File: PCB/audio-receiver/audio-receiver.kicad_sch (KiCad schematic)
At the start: 0 parts

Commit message: create amplifier schematic
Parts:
- added C1: 10uF, symbol Device:C_Polarized
- added C2, C4, C8: 100uF, symbol Device:C_Polarized
- added C3: 100pF, symbol Device:C_Small
- added C5: 2200uF, symbol Device:C_Polarized
- added C6: 33uF, symbol Device:C_Polarized
- added C7: 100nF, symbol Device:C
- added D1, D2, D3, D4: 1N4148, symbol Device:D
- added D5, D6, D7, D8: UF4004, symbol Device:D
- added F1: 1A, symbol Device:Fuse
- added Q1: BC559, Package_TO_SOT_THT:TO-92_Inline, symbol Transistor_BJT:BC559
- added Q2, Q3: BC639, symbol Device:Q_NPN
- added Q4: BC640, symbol Device:Q_PNP
- added Q5: MJE3055, symbol Device:Q_NPN
- added Q6: MJE2955, symbol Device:Q_PNP
- added R1, R2: 33k, symbol Device:R_US
- added R10, R13, R9: 2R7, symbol Device:R_US
- added R11: 12k, symbol Device:R_US
- added R12, R3, R6, R7: 2k2, symbol Device:R_US
- added R4: 100R, symbol Device:R_US
- added R5: 1k, symbol Device:R_US
- added R8: 560, symbol Device:R_US
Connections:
- new net: C8.1, F1.1, Q3.C, Q5.C, R11.2, R6.1
- new net: D1.2 (A), Q3.B, R7.2
- new net: Q3.E, Q5.B, R8.1
- new net: C1.1, Q1.2 (B), R1.2, R2.1
- new net: D6.1 (K), D8.1 (K), Q6.E, R10.2
- new net: C3.2, D4.1 (K), Q2.C, Q4.B
- new net: D3.1 (K), D4.2 (A)
- new net: D5.2 (A), D7.2 (A), Q5.E, R9.1
- new net: C3.1, Q1.1 (C), Q2.B, R5.1
- new net: C2.1, Q1.3 (E), R3.1
- new net: C2.2, R12.1, R4.1
- new net: D2.1 (K), D3.2 (A)
- new net: D1.1 (K), D2.2 (A)
- new net: C6.1, R1.1, R11.1
- new net: Q4.E, Q6.B, R8.2
- new net: C4.1, R6.2, R7.1
- new net: C7.2, R13.1
- new net FB_DC: C4.2, C5.1, D5.1 (K), D6.2 (A), D7.1 (K), D8.2 (A), R10.1, R3.2, R9.2
- new net GND: C6.2, C8.2, Q2.E, Q4.C, Q6.C, R13.2, R2.2, R4.2, R5.2
- new net VCC: F1.2
- new net VIN: C1.2
- new net VOUT: C5.2, C7.1, R12.2
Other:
- note added: "FB_AC"

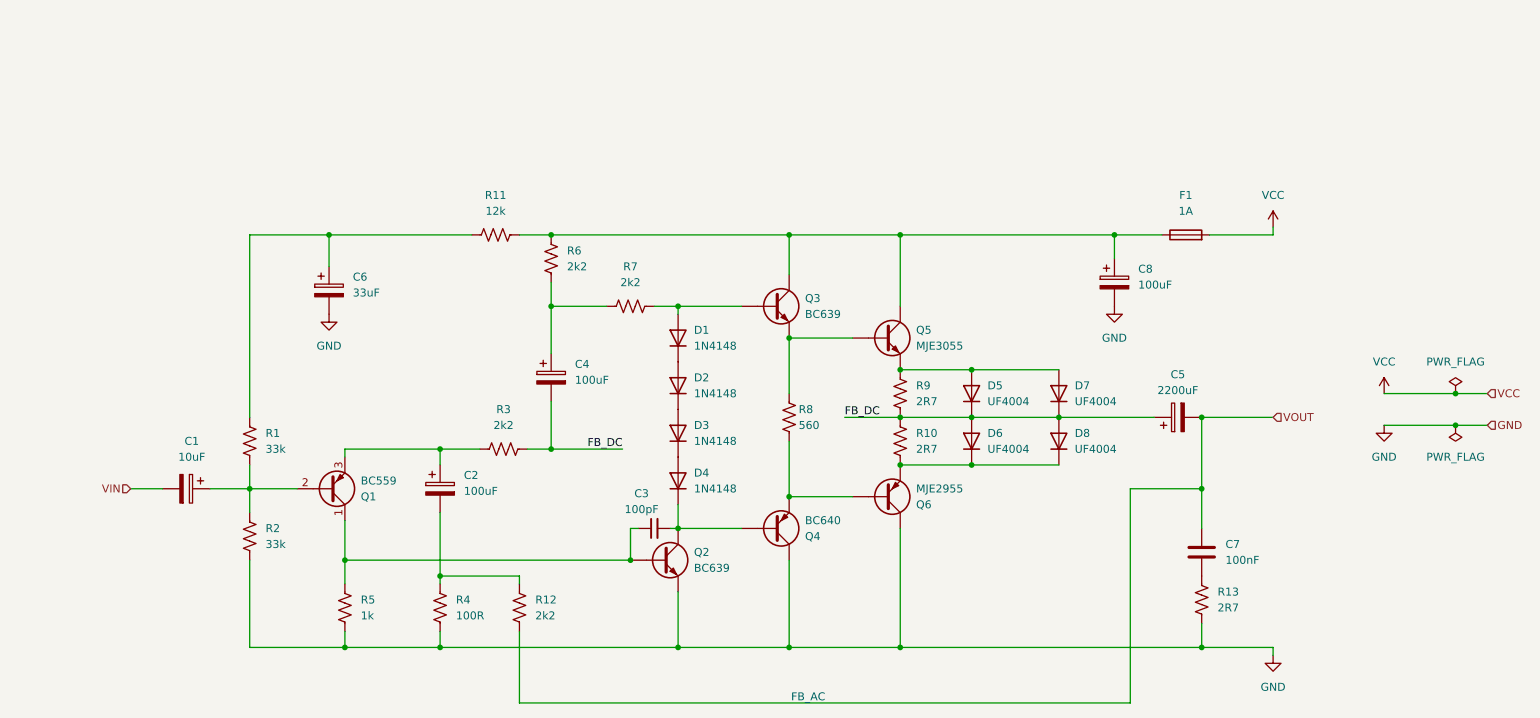
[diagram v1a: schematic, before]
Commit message: edit amplifier schematic
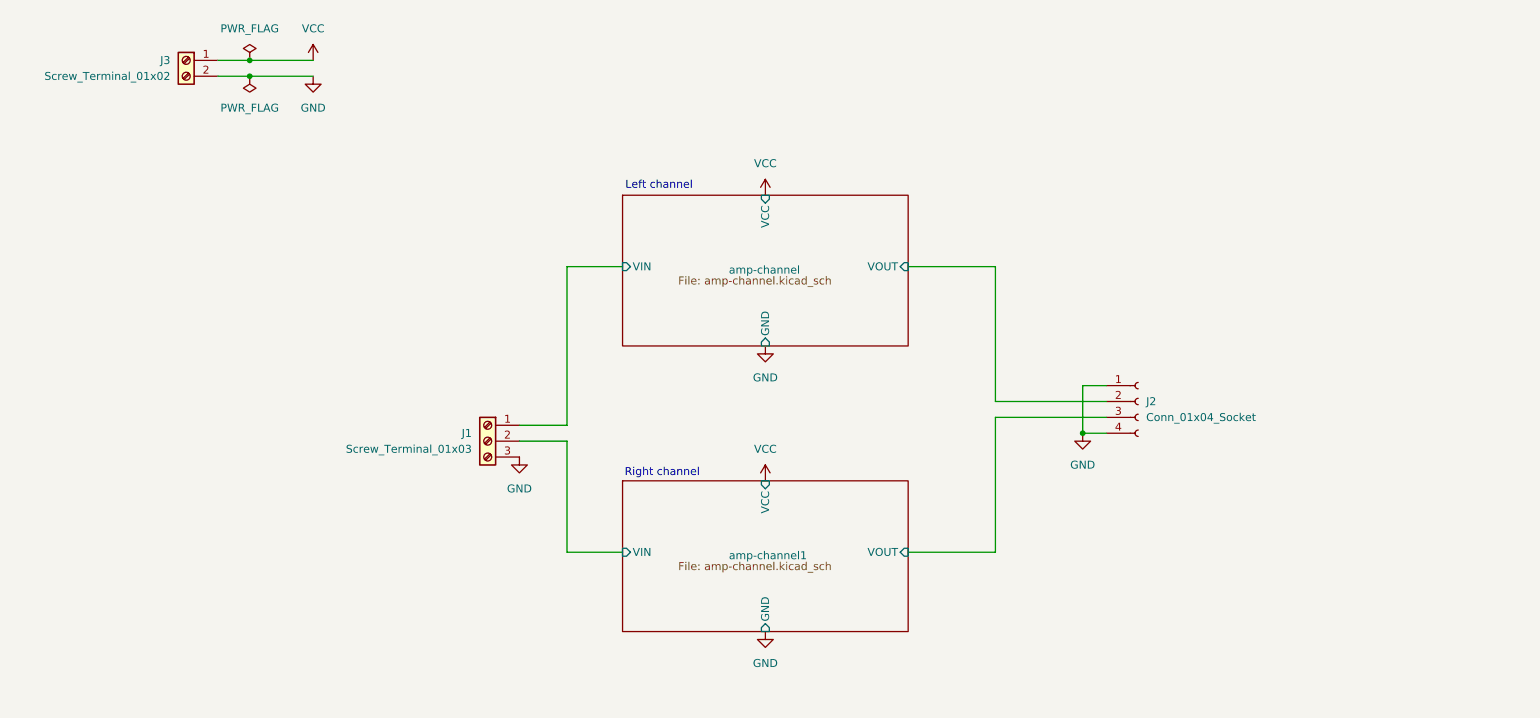
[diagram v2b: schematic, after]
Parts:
- removed C1: 10uF, symbol Device:C_Polarized
- removed C2, C4, C8: 100uF, symbol Device:C_Polarized
- removed C3: 100pF, symbol Device:C_Small
- removed C5: 2200uF, symbol Device:C_Polarized
- removed C6: 33uF, symbol Device:C_Polarized
- removed C7: 100nF, symbol Device:C
- removed D1, D2, D3, D4: 1N4148, symbol Device:D
- removed D5, D6, D7, D8: UF4004, symbol Device:D
- removed F1: 1A, symbol Device:Fuse
- removed Q1: BC559, Package_TO_SOT_THT:TO-92_Inline, symbol Transistor_BJT:BC559
- removed Q2, Q3: BC639, symbol Device:Q_NPN
- removed Q4: BC640, symbol Device:Q_PNP
- removed Q5: MJE3055, symbol Device:Q_NPN
- removed Q6: MJE2955, symbol Device:Q_PNP
- removed R1, R2: 33k, symbol Device:R_US
- removed R10, R13, R9: 2R7, symbol Device:R_US
- removed R11: 12k, symbol Device:R_US
- removed R12, R3, R6, R7: 2k2, symbol Device:R_US
- removed R4: 100R, symbol Device:R_US
- removed R5: 1k, symbol Device:R_US
- removed R8: 560, symbol Device:R_US
- added J1: Screw_Terminal_01x03, symbol Connector:Screw_Terminal_01x03
- added J2: Conn_01x04_Socket, symbol Connector:Conn_01x04_Socket
- added J3: Screw_Terminal_01x02, symbol Connector:Screw_Terminal_01x02
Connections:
- net GND: now also J1.3 (Pin_3), J2.1 (Pin_1), J2.4 (Pin_4), J3.2 (Pin_2)
- net VCC: now also J3.1 (Pin_1)
- new net amp-channel/VIN: J1.1 (Pin_1)
- new net amp-channel/VOUT: J2.2 (Pin_2)
- new net amp-channel1/VIN: J1.2 (Pin_2)
- new net amp-channel1/VOUT: J2.3 (Pin_3)
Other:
- added sheet amp-channel (amp-channel.kicad_sch)
- added sheet amp-channel1 (amp-channel.kicad_sch)
- note added: "Left channel"
- note added: "Right channel"
- note removed: "FB_AC"

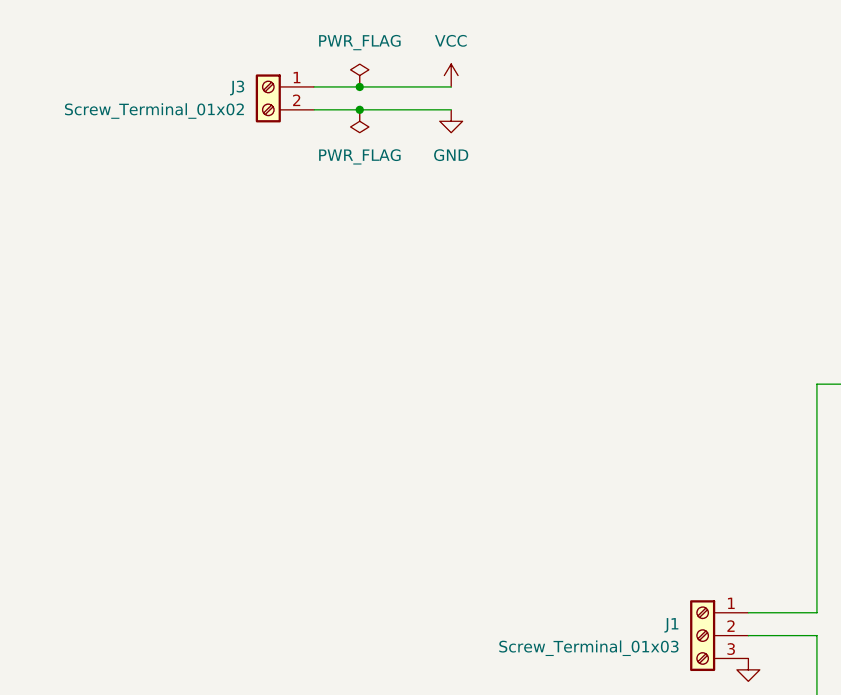
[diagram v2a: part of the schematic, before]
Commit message: update schematic and start work on BOM
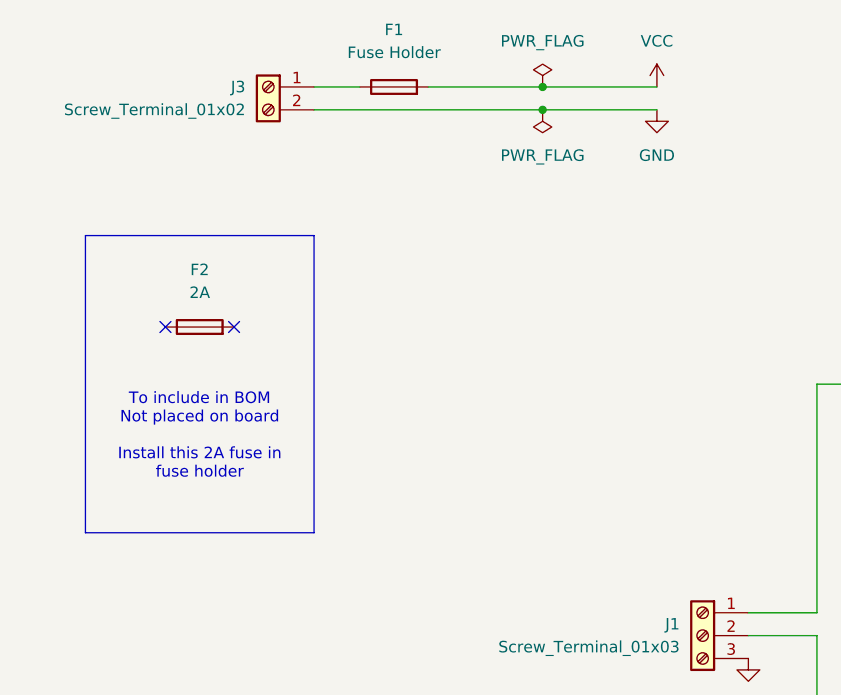
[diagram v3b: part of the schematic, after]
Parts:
- added F1: Fuse Holder, Fuse:Fuseholder_Clip-5x20mm_Eaton_1A5601-01_Inline_P20.80x6.76mm_D1.70mm_Horizontal, symbol Device:Fuse
- added F2: 2A, symbol Device:Fuse
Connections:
- net VCC: now also F1.2; no longer J3.1 (Pin_1)
- new net: F1.1, J3.1 (Pin_1)
- no-connect marks 0 -> 2
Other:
- note added: "To include in BOM Not placed on board Install this 2A fuse in fuse holder"
